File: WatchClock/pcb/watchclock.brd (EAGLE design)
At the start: 100 x 50 mm, 31 parts, among them IC1 MEGA32-A, Q2 BSP170P

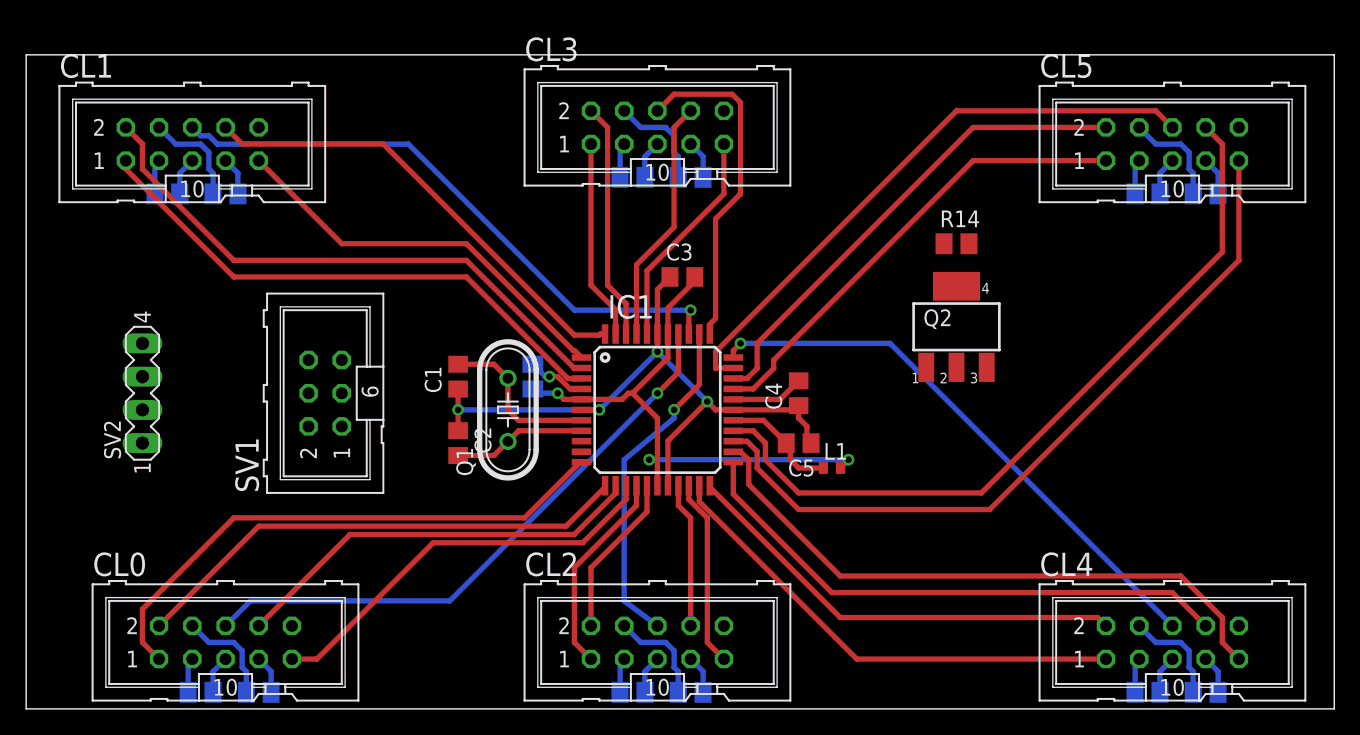
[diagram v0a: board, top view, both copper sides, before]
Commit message: WatchClock PCB: Routing complete
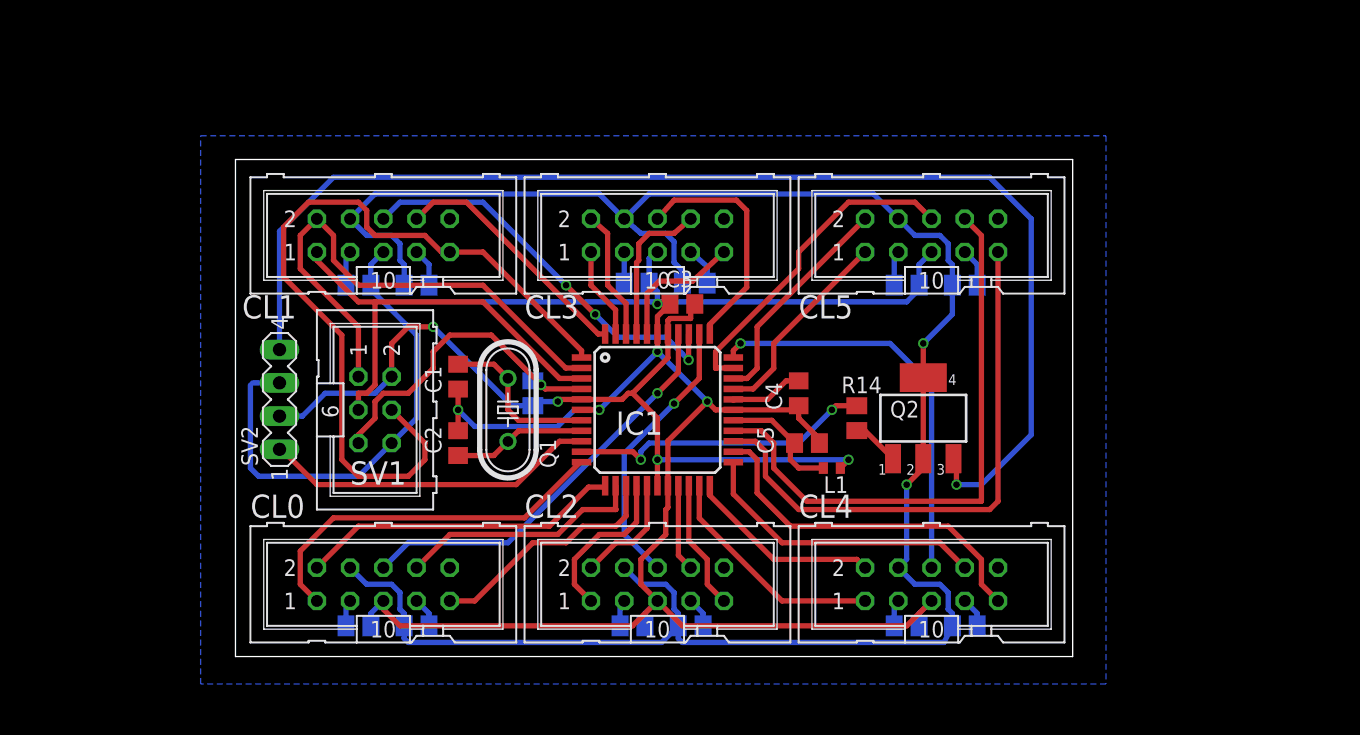
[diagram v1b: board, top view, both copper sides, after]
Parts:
- moved R11 19.7 mm to (71.8, 32.4)
- moved CL5 19.7 mm to (69.2, 36.2)
- moved R7 19.7 mm to (67.3, 32.4)
- moved R10 19.1 mm to (71.8, 6.35)
- moved R4 19.1 mm to (67.3, 6.35)
- moved CL4 18.9 mm to (69.2, 9.53)
- moved CL1 16.2 mm to (27.3, 36.2)
- moved R13 16.2 mm to (29.8, 32.4)
- moved R5 16.2 mm to (25.4, 32.4)
- moved R14 15.4 mm to (63.5, 22.2), turned to 90 degrees
- moved R2 13.1 mm to (25.4, 6.35)
- moved R8 13.1 mm to (29.8, 6.35)
- moved CL0 12.9 mm to (27.3, 9.53)
- moved SV2 10.5 mm to (19.4, 23.7)
- moved CL3 8.26 mm to (48.3, 36.2)
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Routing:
- net GND: track 69.0 -> 201.2 mm, vias 4 -> 5
- net V+: track 47.4 -> 159.3 mm, vias 0 -> 2
- net N$18: track 0.00 -> 95.4 mm, vias 0 -> 1
- net CL1_M2+: track 30.9 -> 61.4 mm
- net RXT: track 0.00 -> 25.6 mm
- net +5V: track 43.6 -> 67.3 mm, vias 3 -> 4
- net N$26: track 0.00 -> 23.4 mm, vias 0 -> 2
- net CL5_ADC: track 45.7 -> 25.1 mm
- net CL5_M1-: track 37.6 -> 17.0 mm
- net CL5_M1+: track 36.1 -> 15.5 mm
- net RESET: track 4.51 -> 24.8 mm
- net CL4_M2-: track 42.7 -> 22.5 mm
- net CL4_M1-: track 34.8 -> 14.9 mm
- net CL4_M2+: track 47.4 -> 27.6 mm
- net CL4_M1+: track 37.3 -> 17.8 mm
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- added copper zone on layer 16, net GND
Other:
- board size 100 x 50 mm -> 64 x 38 mm

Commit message: Update WatchClock PCB
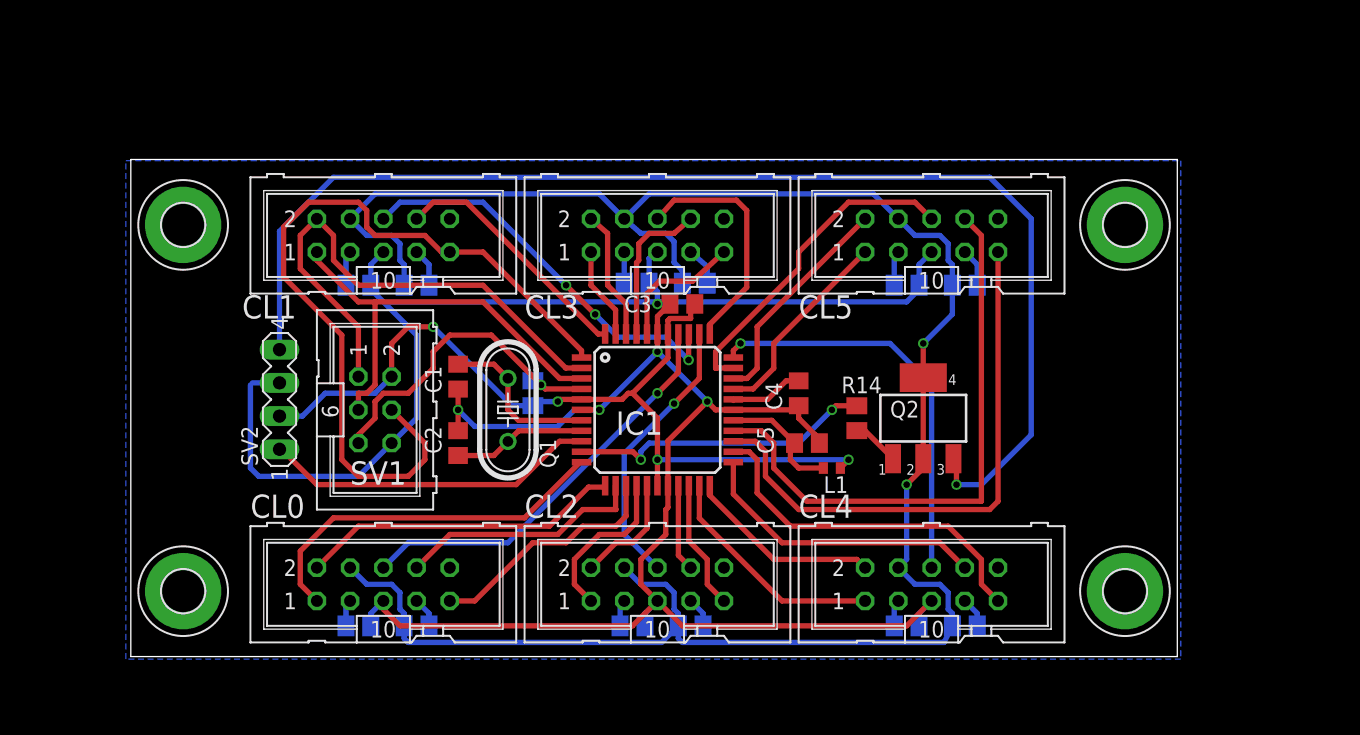
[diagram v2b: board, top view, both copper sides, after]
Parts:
- added H1, H2, H3, H4: MOUNT-PAD-ROUND3.2, holes:3,2-PAD
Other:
- board size 64 x 38 mm -> 80 x 38 mm
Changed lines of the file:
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@@
 <setting verticaltext="up"/>
 </settings>
-<grid distance="25" unitdist="mil" unit="mil" style="lines" multiple="1" display="no" altdistance="0.025" altunitdist="inch" altunit="inch"/>
+<grid distance="0.635" unitdist="mm" unit="mm" style="lines" multiple="1" display="no" altdistance="0.025" altunitdist="inch" altunit="inch"/>
 <layers>
 <layer number="1" name="Top" color="4" fill="1" visible="yes" active="yes"/>
@@
 <board>
 <plain>
-<wire x1="16" y1="4" x2="80" y2="4" width="0" layer="20"/>
-<wire x1="80" y1="4" x2="80" y2="42" width="0" layer="20"/>
-<wire x1="80" y1="42" x2="16" y2="42" width="0" layer="20"/>
-<wire x1="16" y1="42" x2="16" y2="4" width="0" layer="20"/>
+<wire x1="8" y1="4" x2="88" y2="4" width="0" layer="20"/>
+<wire x1="88" y1="4" x2="88" y2="42" width="0" layer="20"/>
+<wire x1="88" y1="42" x2="8" y2="42" width="0" layer="20"/>
+<wire x1="8" y1="42" x2="8" y2="4" width="0" layer="20"/>
 </plain>
 <attributes>
@@
 <attribute name="VALUE" x="30.48" y="21.59" size="1.27" layer="27" rot="R270"/>
 </element>
-<element name="C3" library="resistor" package="C0805" value="100n" x="50.165" y="30.95625"/>
+<element name="C3" library="resistor" package="C0805" value="100n" x="50.165" y="30.95625" smashed="yes">
+<attribute name="NAME" x="45.72" y="30.32125" size="1.27" layer="25"/>
+<attribute name="VALUE" x="48.895" y="28.41625" size="1.27" layer="27"/>
+</element>
 <element name="C4" library="resistor" package="C0805" value="100n" x="59.055" y="24.13" rot="R90"/>
 <element name="C5" library="resistor" package="C0805" value="100n" x="59.69" y="20.32" smashed="yes" rot="R180">
@@
 <attribute name="OC_FARNELL" value="unknown" x="19.3675" y="23.65375" size="1.778" layer="27" rot="R90" display="off"/>
 </element>
+<element name="H1" library="holes" package="3,2-PAD" value="MOUNT-PAD-ROUND3.2" x="12" y="9"/>
+<element name="H2" library="holes" package="3,2-PAD" value="MOUNT-PAD-ROUND3.2" x="84" y="9"/>
+<element name="H3" library="holes" package="3,2-PAD" value="MOUNT-PAD-ROUND3.2" x="12" y="37"/>
+<element name="H4" library="holes" package="3,2-PAD" value="MOUNT-PAD-ROUND3.2" x="84" y="37"/>
 </elements>
 <signals>
@@
 <wire x1="60.325" y1="20.635" x2="60.64" y2="20.32" width="0.4064" layer="1"/>
 <polygon width="0.4064" layer="16">
-<vertex x="13.335" y="43.815"/>
-<vertex x="82.55" y="43.815"/>
-<vertex x="82.55" y="1.905"/>
-<vertex x="13.335" y="1.905"/>
+<vertex x="7.62" y="41.91"/>
+<vertex x="88.265" y="41.91"/>
+<vertex x="88.265" y="3.81"/>
+<vertex x="7.62" y="3.81"/>
 </polygon>
 </signal>
